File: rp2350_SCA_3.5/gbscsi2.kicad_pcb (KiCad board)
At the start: 4 copper layers, 100 x 93.6 mm, 105 parts, among them J1 USB_DATA, J2 TF003, J3 Conn_01x02, J6 Conn_01x05, J7 Conn_01x04, J8 Conn_01x02, J9 Conn_02x40_Counter_Clockwise, SW1 SW_DIP_x03, U1 RP2350_80QFN, U10 W25Q128JVS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

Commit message: Re-sorting things around
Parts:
- SW1: footprint Button_Switch_SMD:SW_DIP_SPSTx04_Slide_6.7x11.72mm_W8.61mm_P2.54mm_LowProfile -> Button_Switch_SMD:SW_DIP_SPSTx03_Slide_6.7x9.18mm_W8.61mm_P2.54mm_LowProfile
- moved SW1 1.40 mm to (102.4, 123.0)
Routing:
- net /~{USB_BOOT}: track 54.3 -> 51.3 mm
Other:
- board text added: "2350W"
- board text added: "3.5{dblquote} FWSCSI-SCA pcb v0.1"
- board text removed: "GBSCSI2 2350 WIDE SCA pcb v0.1"

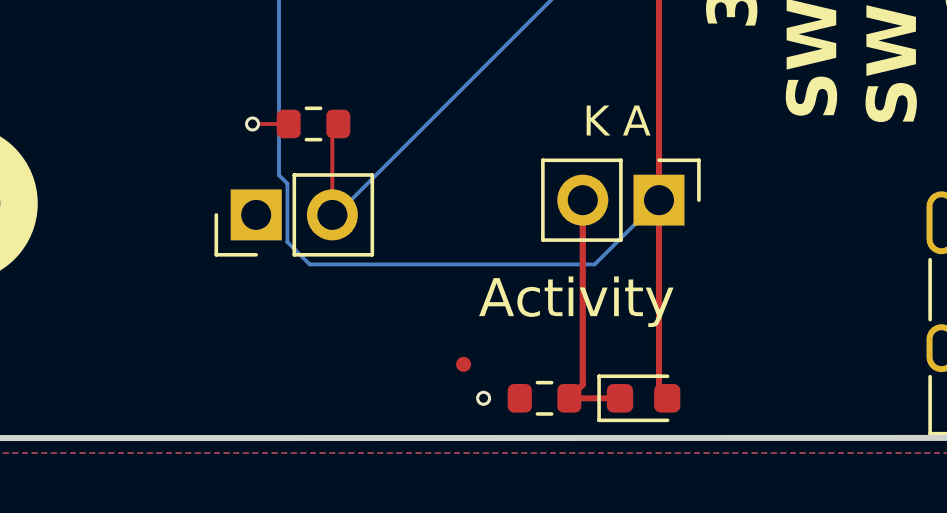
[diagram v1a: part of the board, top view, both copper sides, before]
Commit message: Attempting to organize sheet details, adding eject buttons to Wide variants
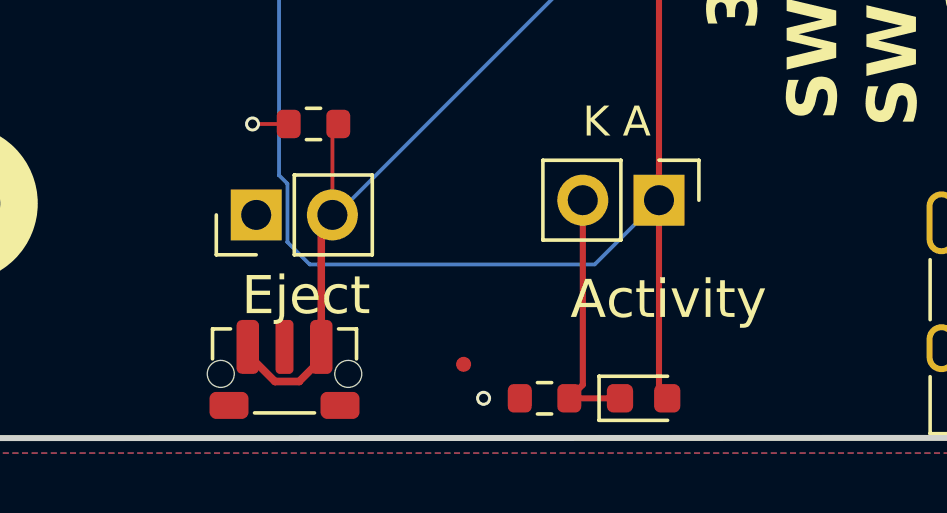
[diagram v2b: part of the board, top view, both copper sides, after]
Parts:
- added SW2: GT-TC108A-H034-L1S, GBSCSI:SW_Push_1P1T-MP_NO_Horizontal_Alps_SKRTLAE010, F.Cu at (40.3, 128.7)
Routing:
- net /EJECT: track 41.3 -> 49.6 mm
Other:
- board text added: "Eject"

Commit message: Cleaning up, updating docs
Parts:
- C1: value 100nF -> 10uF
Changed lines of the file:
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@@
     (descr "Capacitor SMD 0603 (1608 Metric), square (rectangular) end terminal, IPC_7351 nominal, (Body size source: IPC-SM-782 page 76, https://www.pcb-3d.com/wordpress/wp-content/uploads/ipc-sm-782a_amendment_1_and_2.pdf), generated with kicad-footprint-generator")
     (tags "capacitor")
-    (property "LCSC" "C14663")
-    (property "LCSC Part #" "C14663")
+    (property "LCSC" "C96446")
+    (property "LCSC Part #" "C96446")
     (property "Sheetfile" "gbscsi2.kicad_sch")
     (property "Sheetname" "")
@@
         (effects (font (size 1 1) (thickness 0.15)))
     )
-    (fp_text value "100nF" (at 0 1.43 -270) (layer "F.Fab")
+    (fp_text value "10uF" (at 0 1.43 -270) (layer "F.Fab")
         (effects (font (size 1 1) (thickness 0.15)))
     )
